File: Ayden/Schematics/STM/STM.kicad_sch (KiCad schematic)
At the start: 2 parts

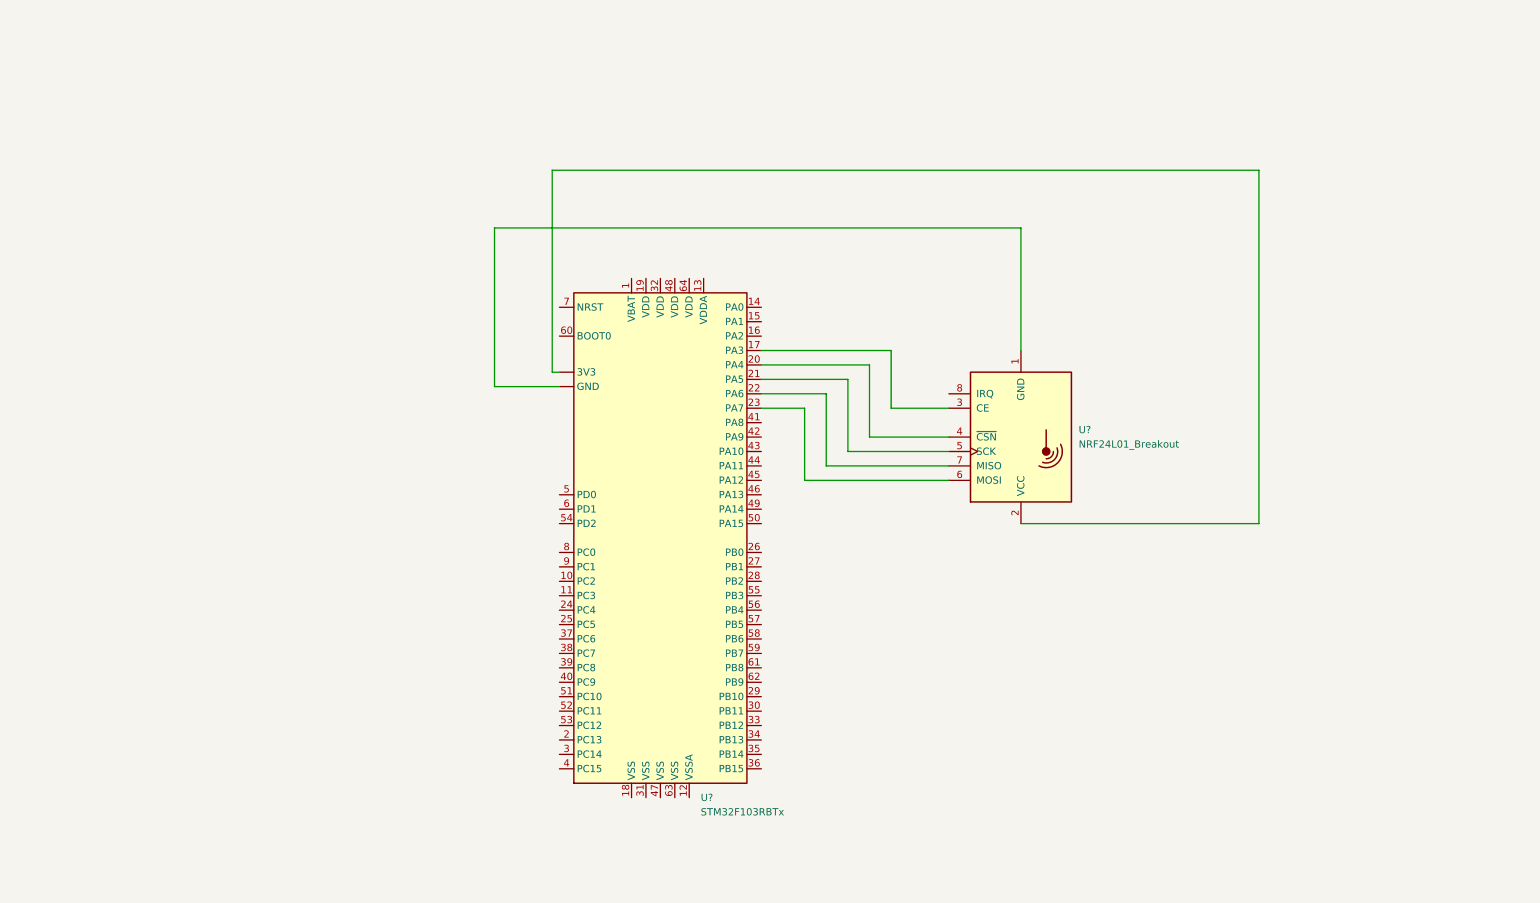
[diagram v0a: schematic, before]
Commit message: Added prototype 3x3 pressure mat to STM schematic
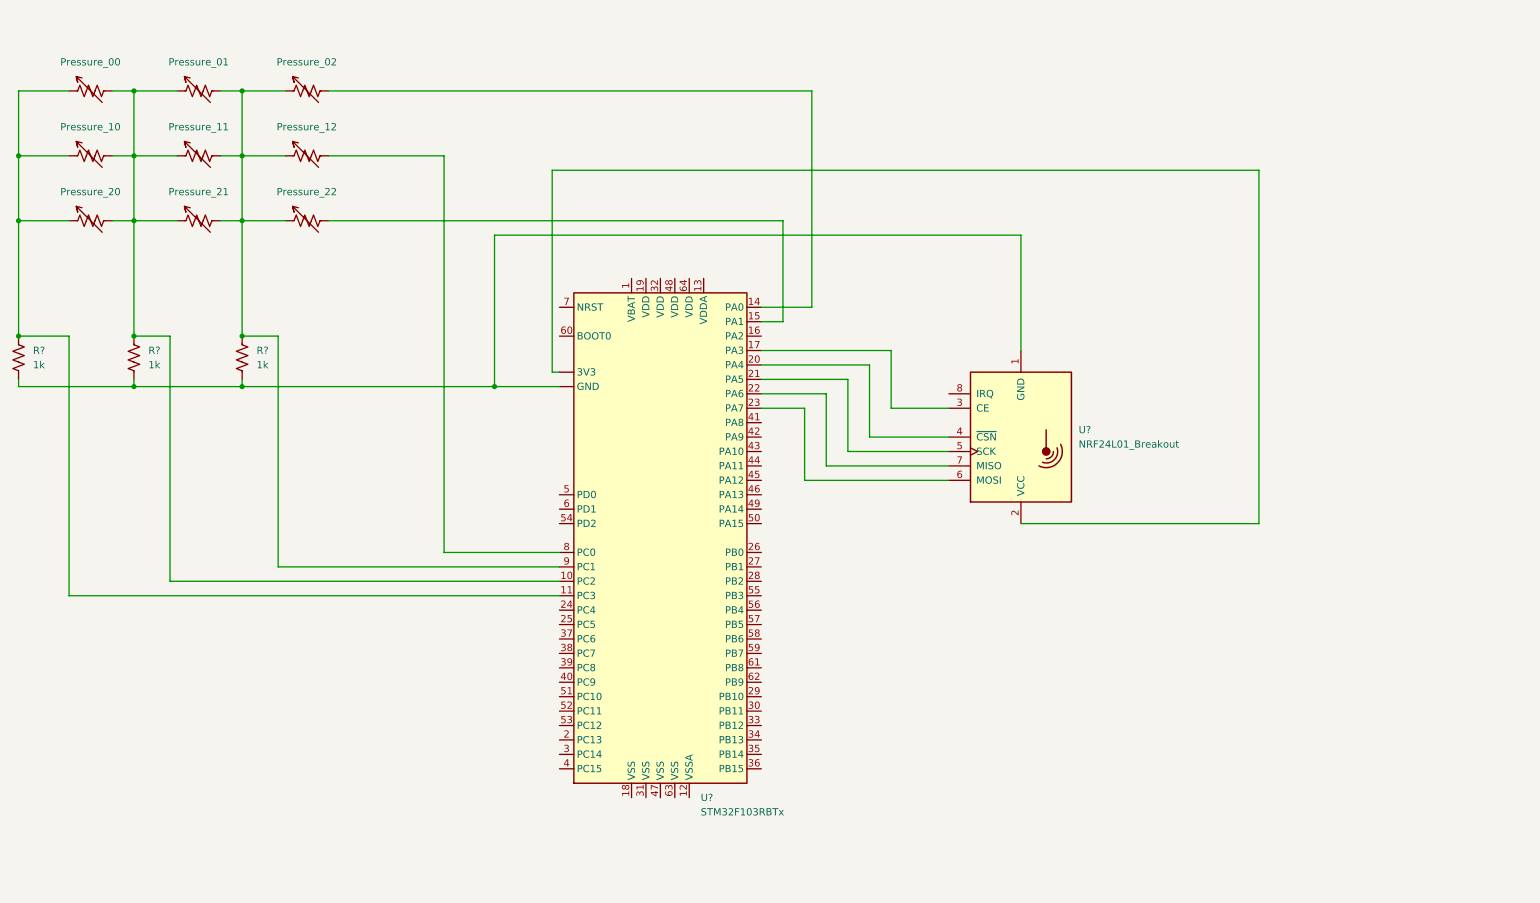
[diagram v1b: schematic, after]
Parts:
- added Pressure_00, Pressure_01, Pressure_02, Pressure_10, Pressure_11, Pressure_12, Pressure_20, Pressure_21, Pressure_22: R, symbol Device:R_Variable_US
- added R? (x3): 1k, symbol Device:R_US
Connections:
- net at U?. (GND), U?.1 (GND): now also R?.1, R?.1, R?.1
- net at U?.10 (PC2): now also Pressure_00.2, Pressure_01.1, Pressure_10.2, Pressure_11.1, Pressure_20.2, Pressure_21.1, R?.2
- net at U?.11 (PC3): now also Pressure_00.1, Pressure_10.1, Pressure_20.1, R?.2
- net at U?.14 (PA0): now also Pressure_02.2
- net at U?.15 (PA1): now also Pressure_22.2
- net at U?.8 (PC0): now also Pressure_12.2
- net at U?.9 (PC1): now also Pressure_01.2, Pressure_02.1, Pressure_11.2, Pressure_12.1, Pressure_21.2, Pressure_22.1, R?.2

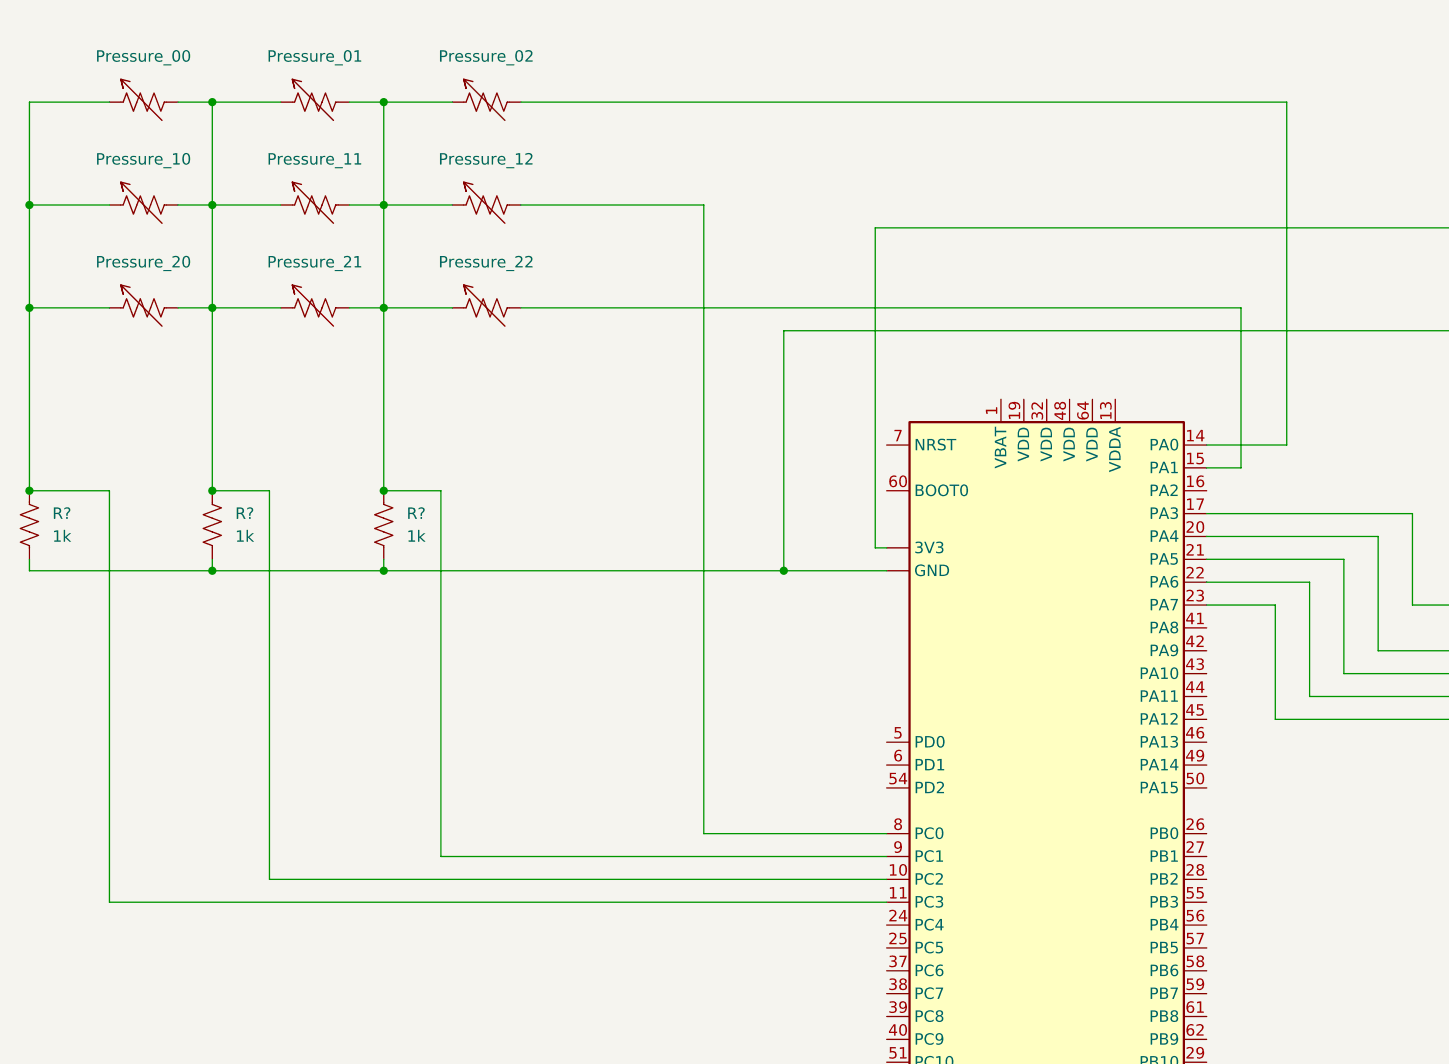
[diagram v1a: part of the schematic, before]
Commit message: Edited schematic to reflect new pull-up configuration
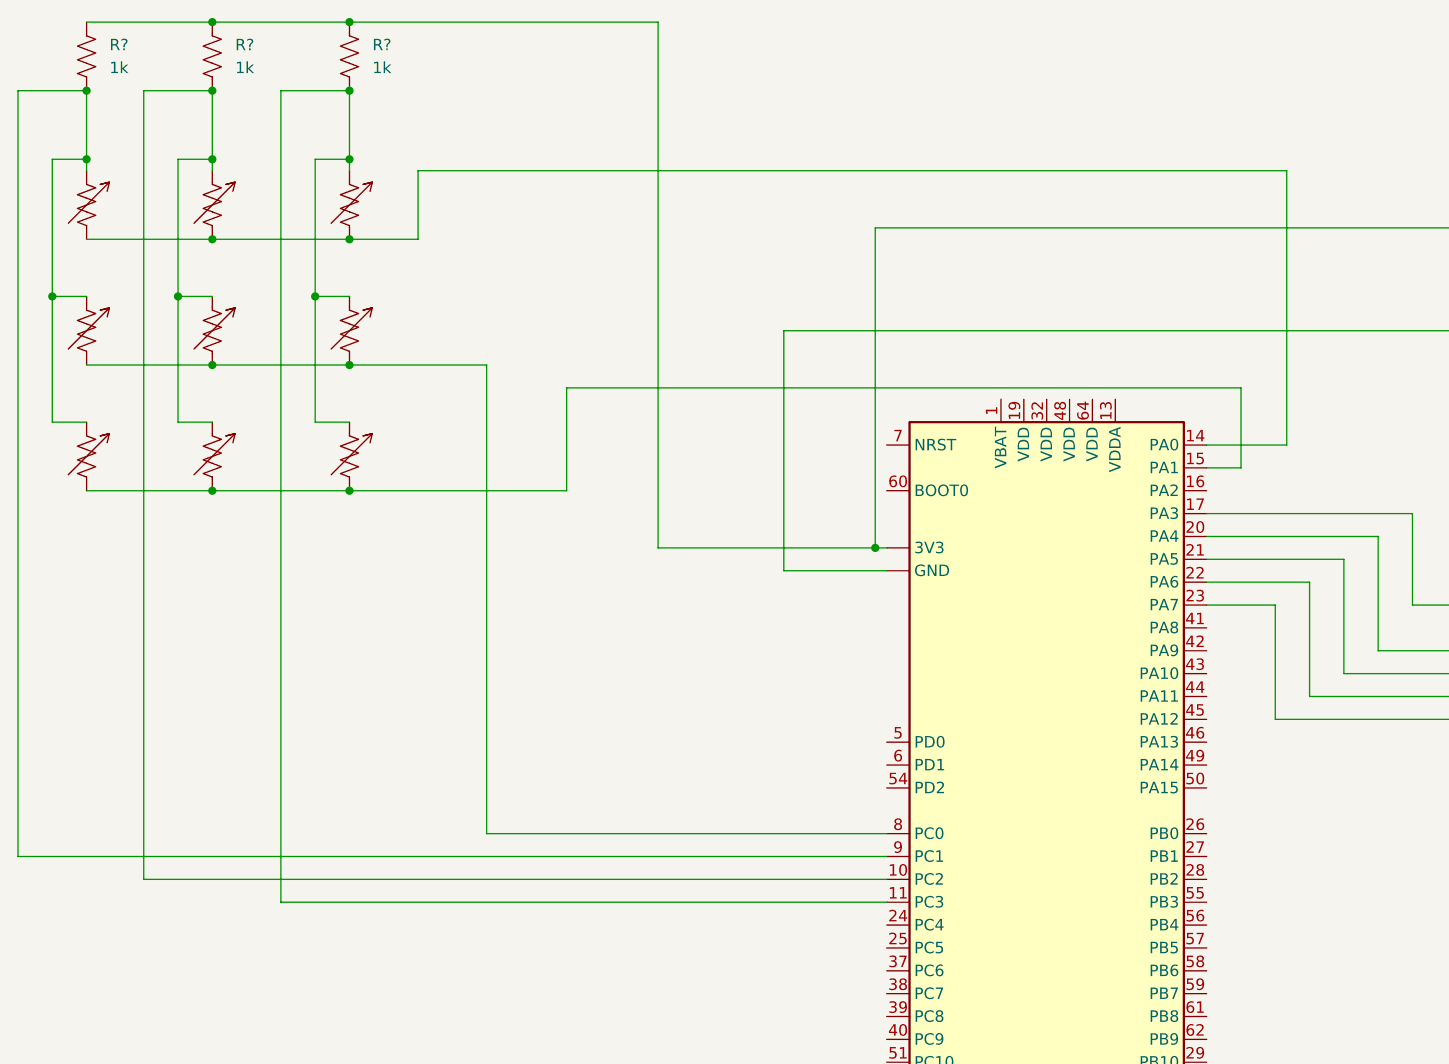
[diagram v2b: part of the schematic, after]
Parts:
- removed Pressure_00, Pressure_01, Pressure_02, Pressure_10, Pressure_11, Pressure_12, Pressure_20, Pressure_21, Pressure_22: R, symbol Device:R_Variable_US
- added R? (x9): R_Variable_US, symbol Device:R_Variable_US
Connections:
- net at U?.11 (PC3): now also R?.1, R?.1, R?.1, R?.1; no longer R?.2
- net at U?.10 (PC2): now also R?.1, R?.1, R?.1, R?.1; no longer R?.2
- net at U?.9 (PC1): now also R?.1, R?.1, R?.1, R?.1; no longer R?.2
- net at U?.14 (PA0): now also R?.2, R?.2, R?.2
- net at U?. (GND), U?.2 (VCC): now also R?.2, R?.2, R?.2
- net at U?.15 (PA1): now also R?.2, R?.2, R?.2
- net at U?.8 (PC0): now also R?.2, R?.2, R?.2
- new net: U?. (GND), U?.1 (GND)
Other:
- moved on the sheet: R?

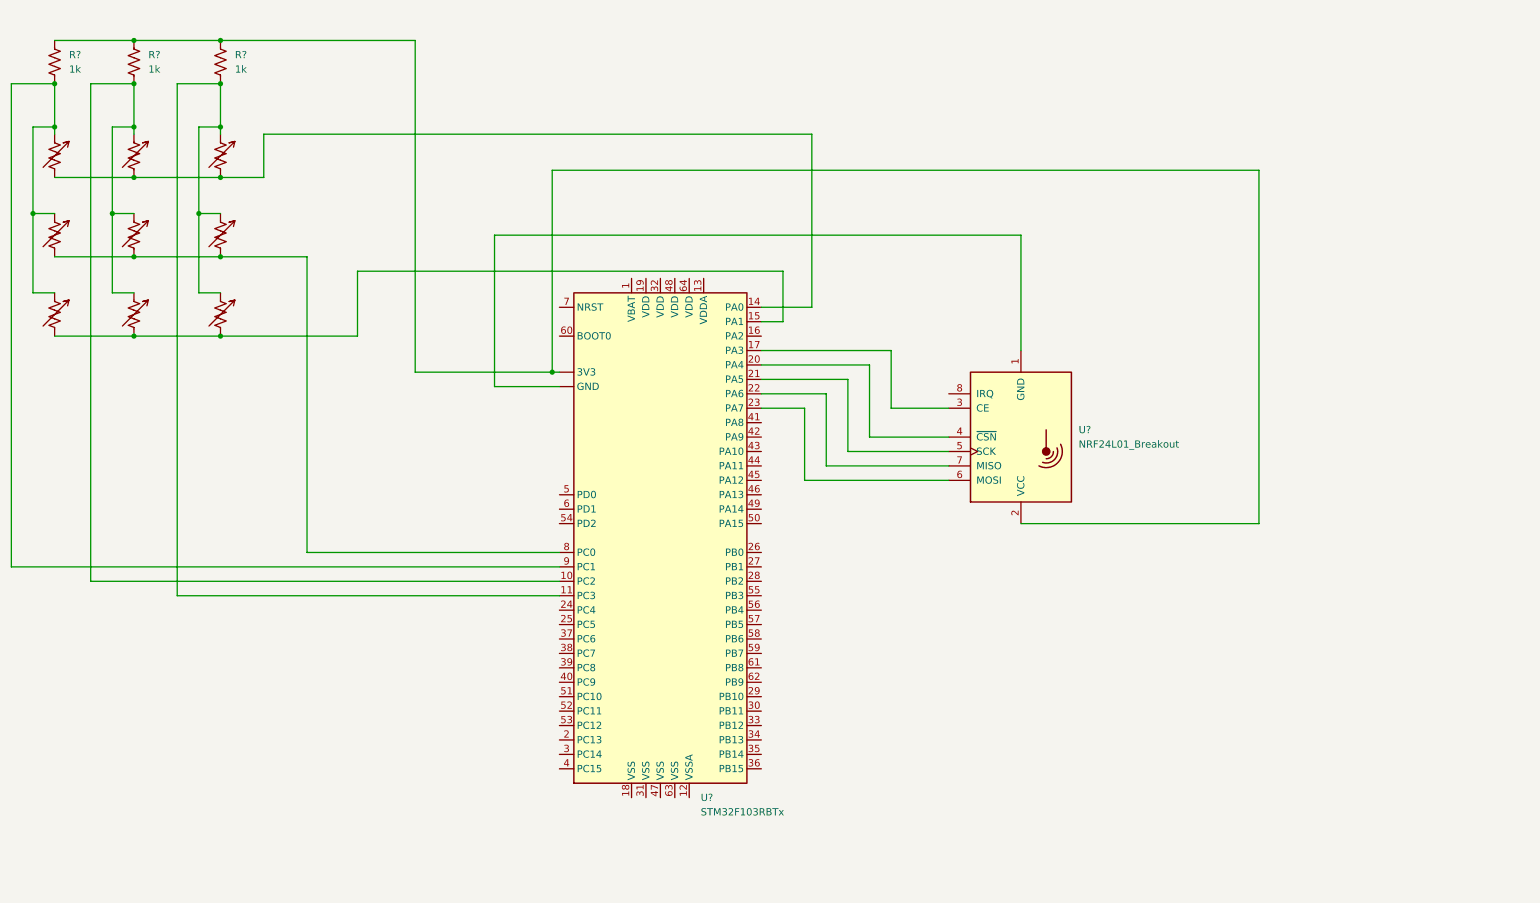
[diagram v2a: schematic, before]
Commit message: Updated schematic to include full-size pressure mat
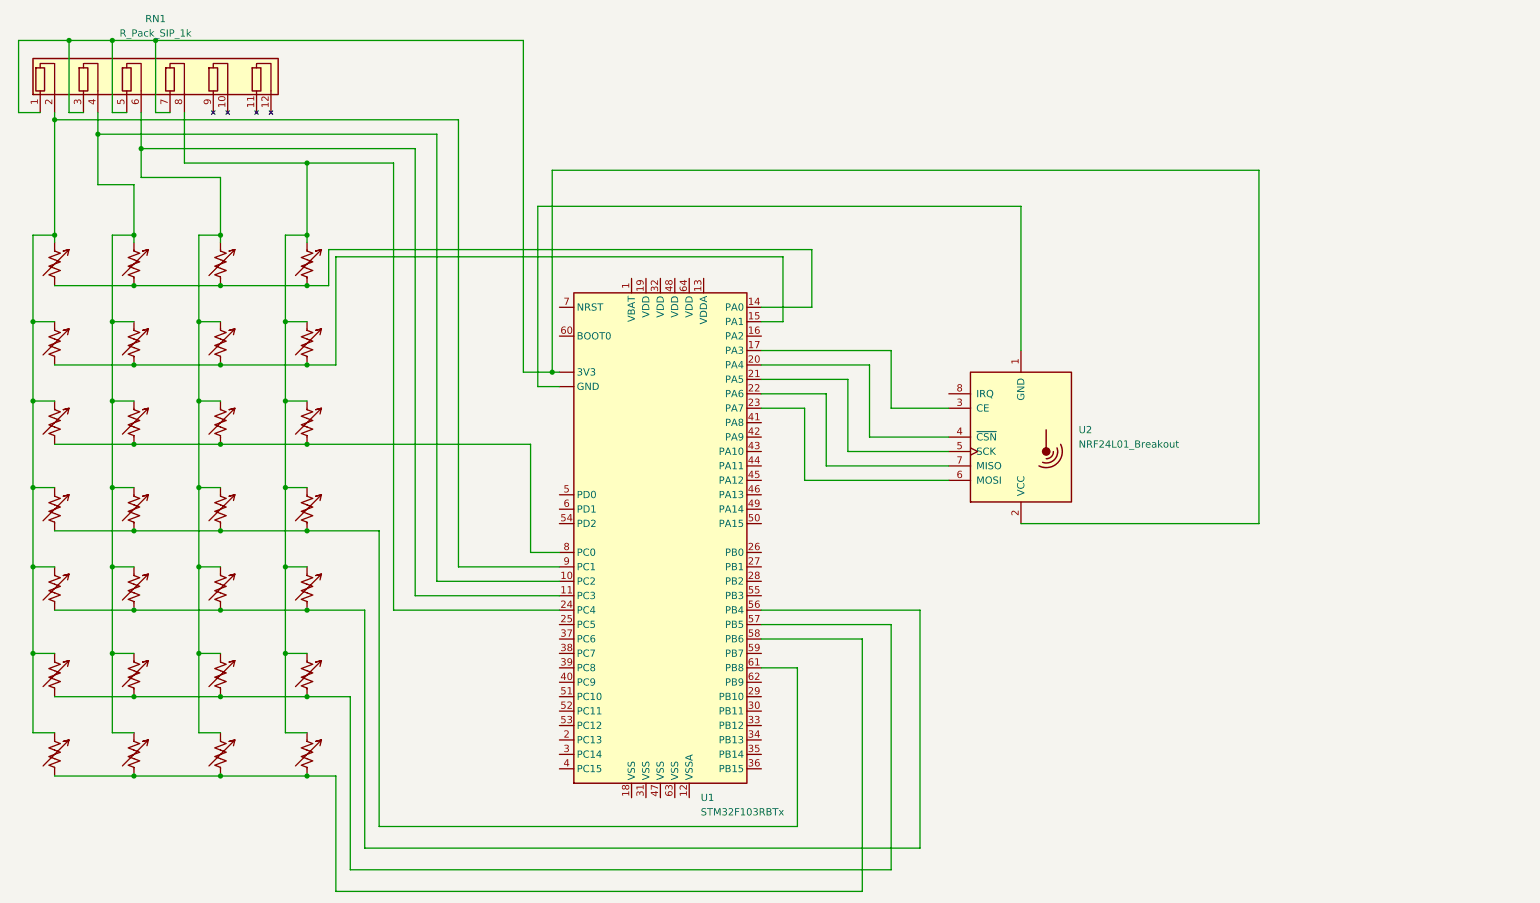
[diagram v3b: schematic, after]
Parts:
- removed R? (x3): 1k, symbol Device:R_US
- added R? (x19): R_Variable_US, symbol Device:R_Variable_US
- added RN1: R_Pack_SIP_1k, Resistor_THT:R_Array_SIP12, symbol Device:R_Pack06_SIP
- gave numbers to parts that had none: 2
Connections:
- net at R?.1, R?.1, R?.1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: now also R?.1, R?.1, R?.1, R?.1, RN1.2 (R1.2)
- net at R?.2, R?.2, R?.2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: now also R?.2
- net at R?.1, R?.1, R?.1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: now also R?.1, R?.1, R?.1, R?.1, RN1.4 (R2.2)
- net at R?.2, R?.2, R?.2: now also U1.15 (PA1), R?.2; no longer U1.8 (PC0)
- net at R?.1, R?.1, R?.1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: now also R?.1, R?.1, R?.1, R?.1, RN1.6 (R3.2)
- net at U1. (GND), U2.2 (VCC): now also RN1.1 (R1.1), RN1.3 (R2.1), RN1.5 (R3.1), RN1.7 (R4.1)
- net at R?.2, R?.2, R?.2: now also U1.8 (PC0), R?.2; no longer U1.15 (PA1)
- net at U1.24 (PC4): now also R?.1, R?.1, R?.1, R?.1, R?.1, R?.1, R?.1, RN1.8 (R4.2)
- net at U1.56 (PB4): now also R?.2, R?.2, R?.2, R?.2
- net at U1.57 (PB5): now also R?.2, R?.2, R?.2, R?.2
- net at U1.58 (PB6): now also R?.2, R?.2, R?.2, R?.2
- net at U1.61 (PB8): now also R?.2, R?.2, R?.2, R?.2
